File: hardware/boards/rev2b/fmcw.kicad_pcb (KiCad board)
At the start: 4 copper layers, 118.6 x 62 mm, 445 parts, among them CON1 BARREL_JACK, J1 SD_Card, J2 USB_B_Micro, J3 SMA, J4 SMA, J5 SMA, J6 Conn_02x08_Odd_Even, Q1 DNP(RE1C002UN), Q2 RE1C002UN, SW1 SW_PUSH, T1 uwave, T10 uwave, T11 uwave, T12 uwave, T13 uwave, T14 uwave, T15 uwave, T16 uwave, T2 uwave, T3 uwave, T4 uwave, T5 uwave, T6 uwave, T7 uwave, T8 uwave, T9 uwave, U1 LP5907MFX-3.3, U10 LP5907MFX-3.0, U11 LTC2292, U12 ADF4158, U13 TLV172DCK, U14 PS2012GT2-R50, U15 HMC431, U17 PAT1220-C-2DB, U18 SE5004L, U2 LP5907MFX-1.8, U20 PAT1220-C-6DB, U21 LMV321, U22 TRF37A73, U23 SKY65404, U24 TRF37A73, U25 SKY65404, U26 L7980, U27 L7980, U28 L7980, U29 LP2985A-10DBVR, U3 KT2520K-T, U30 TPS7A91, U31 TPS7A91, U32 TPS7A91, U33 LP5907MFX-3.0, U34 TPS7A91, U35 5400BL15B050E, U36 5400BL15B050E, U37 5400BL15B050E, U38 ADL5802, U39 ADA4940-2, U4 NC7SVU04P5X, U40 TPS7A91, U5 NB3N551, U6 XC7A15T-FTG256, U7 MX25L3233F, U8 93LCxxBxxOT, U9 FT2232H, Y1 12MHz

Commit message: rev2b: place silkscreen
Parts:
- moved R21 0.40 mm to (87.5, 105.1)
- moved R20 0.40 mm to (87.5, 104.1)
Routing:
- net /3V3D: track 279.4 -> 280.8 mm
- net GND: vias 901 -> 907

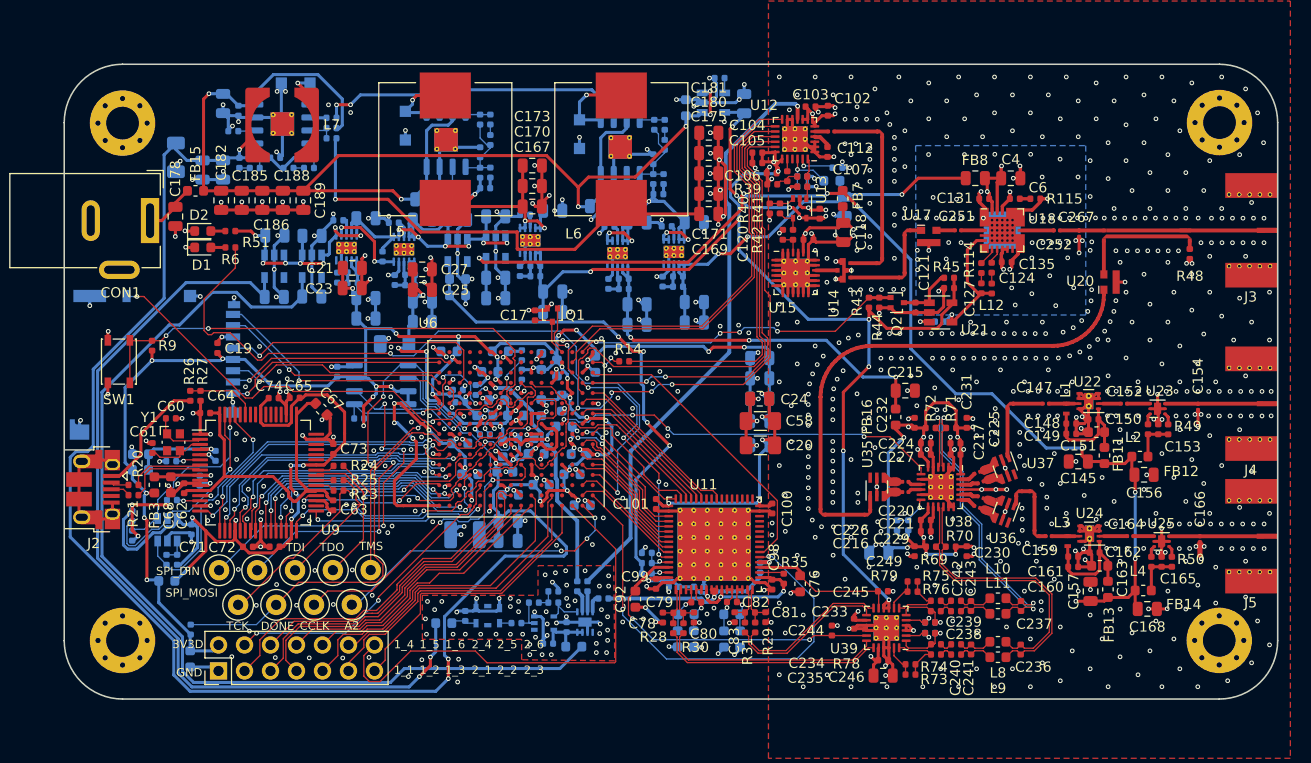
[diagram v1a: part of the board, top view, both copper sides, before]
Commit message: rev2b: add via perimeter
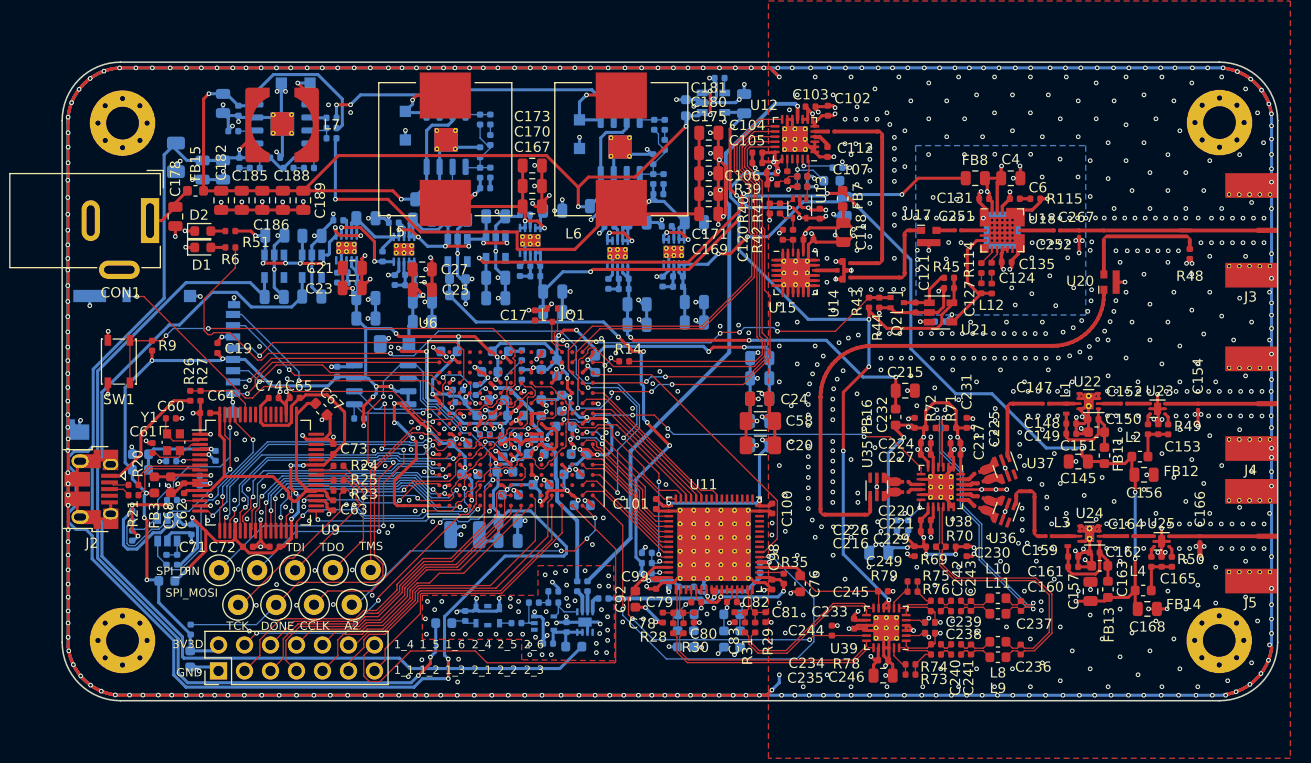
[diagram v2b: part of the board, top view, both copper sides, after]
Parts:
- moved J2 0.17 mm to (83.4, 104.5)
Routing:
- net GND: track 628.9 -> 1189.1 mm, vias 907 -> 1126
- net Net-(C5-Pad1): track 97.9 -> 96.3 mm
- net /1V0: track 165.8 -> 167.0 mm
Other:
- board size 118.6 x 62 mm -> 118.8 x 62.4 mm

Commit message: rev2b: update pcb cost dwg
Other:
- board text added: "PCB cost (OshPark 4-layer): $10/sq.in. x 2.46in. x 4.68in. = $115"
- board text removed: "PCB cost (OshPark 4-layer): $10/sq.in. x 3.28in. x 4.67in. = $153"
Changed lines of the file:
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@@
   (general
     (thickness 1.6002)
-    (drawings 88)
+    (drawings 86)
     (tracks 6130)
     (zones 0)
@@
     (38 B.Mask user hide)
     (39 F.Mask user hide)
-    (40 Dwgs.User user hide)
+    (40 Dwgs.User user)
     (41 Cmts.User user hide)
     (42 Eco1.User user hide)
@@
   (gr_arc (start 193.63 119.45) (end 193.63 125.15) (angle -90) (layer Edge.Cuts) (width 0.15))
   (gr_arc (start 193.63 68.45) (end 199.33 68.45) (angle -90) (layer Edge.Cuts) (width 0.15))
-  (dimension 118.604099 (width 0.127) (layer Dwgs.User)
-    (gr_text "4.6695 in" (at 131.652049 287.8422) (layer Dwgs.User)
-      (effects (font (size 0.8382 0.8382) (thickness 0.127)))
-    )
-    (feature1 (pts (xy 190.954099 265.057269) (xy 190.954099 287.336421)))
-    (feature2 (pts (xy 72.35 265.057269) (xy 72.35 287.336421)))
-    (crossbar (pts (xy 72.35 286.75) (xy 190.954099 286.75)))
-    (arrow1a (pts (xy 190.954099 286.75) (xy 189.827595 287.336421)))
-    (arrow1b (pts (xy 190.954099 286.75) (xy 189.827595 286.163579)))
-    (arrow2a (pts (xy 72.35 286.75) (xy 73.476504 287.336421)))
-    (arrow2b (pts (xy 72.35 286.75) (xy 73.476504 286.163579)))
-  )
-  (dimension 62 (width 0.127) (layer Dwgs.User)
-    (gr_text "2.4409 in" (at 211.646154 242.35 270) (layer Dwgs.User)
-      (effects (font (size 0.8382 0.8382) (thickness 0.127)))
-    )
-    (feature1 (pts (xy 184.95 273.35) (xy 211.140375 273.35)))
-    (feature2 (pts (xy 184.95 211.35) (xy 211.140375 211.35)))
-    (crossbar (pts (xy 210.553954 211.35) (xy 210.553954 273.35)))
-    (arrow1a (pts (xy 210.553954 273.35) (xy 209.967533 272.223496)))
-    (arrow1b (pts (xy 210.553954 273.35) (xy 211.140375 272.223496)))
-    (arrow2a (pts (xy 210.553954 211.35) (xy 209.967533 212.476504)))
-    (arrow2b (pts (xy 210.553954 211.35) (xy 211.140375 212.476504)))
-  )
   (gr_arc (start 86.25 119.45) (end 80.55 119.45) (angle -90) (layer Edge.Cuts) (width 0.15))
   (gr_arc (start 86.25 68.45) (end 86.25 62.75) (angle -90) (layer Edge.Cuts) (width 0.15))
@@
   (gr_line (start 159.654099 90.475262) (end 177.449099 90.475262) (layer F.Mask) (width 0.78))
   (gr_line (start 160.679099 69.985262) (end 160.679099 81.865) (layer F.Mask) (width 0.78))
-  (dimension 118.604099 (width 0.127) (layer Dwgs.User)
-    (gr_text "4.6695 in" (at 137.552049 142.470193) (layer Dwgs.User)
+  (dimension 118.8 (width 0.127) (layer Dwgs.User)
+    (gr_text "4.6772 in" (at 139.95 142.470193) (layer Dwgs.User)
       (effects (font (size 0.8382 0.8382) (thickness 0.127)))
     )
-    (feature1 (pts (xy 196.854099 119.685262) (xy 196.854099 141.964414)))
-    (feature2 (pts (xy 78.25 119.685262) (xy 78.25 141.964414)))
-    (crossbar (pts (xy 78.25 141.377993) (xy 196.854099 141.377993)))
-    (arrow1a (pts (xy 196.854099 141.377993) (xy 195.727595 141.964414)))
-    (arrow1b (pts (xy 196.854099 141.377993) (xy 195.727595 140.791572)))
-    (arrow2a (pts (xy 78.25 141.377993) (xy 79.376504 141.964414)))
-    (arrow2b (pts (xy 78.25 141.377993) (xy 79.376504 140.791572)))
+    (feature1 (pts (xy 199.35 119.685262) (xy 199.35 141.964414)))
+    (feature2 (pts (xy 80.55 119.685262) (xy 80.55 141.964414)))
+    (crossbar (pts (xy 80.55 141.377993) (xy 199.35 141.377993)))
+    (arrow1a (pts (xy 199.35 141.377993) (xy 198.223496 141.964414)))
+    (arrow1b (pts (xy 199.35 141.377993) (xy 198.223496 140.791572)))
+    (arrow2a (pts (xy 80.55 141.377993) (xy 81.676504 141.964414)))
+    (arrow2b (pts (xy 80.55 141.377993) (xy 81.676504 140.791572)))
   )
-  (gr_text "PCB cost (OshPark 4-layer):\n$10/sq.in. x 3.28in. x 4.67in. = $153" (at 78.72 31.17) (layer Dwgs.User)
+  (gr_text "PCB cost (OshPark 4-layer):\n$10/sq.in. x 2.46in. x 4.68in. = $115" (at 101.15 52.65) (layer Dwgs.User)
     (effects (font (size 0.8382 0.8382) (thickness 0.127)))
   )
-  (dimension 83.295 (width 0.127) (layer Dwgs.User)
-    (gr_text "3.279330709 in" (at 231.741264 85.237762 270) (layer Dwgs.User)
+  (dimension 62.4 (width 0.127) (layer Dwgs.User)
+    (gr_text "2.4567 in" (at 231.741264 93.95 270) (layer Dwgs.User)
       (effects (font (size 0.8382 0.8382) (thickness 0.127)))
     )
-    (feature1 (pts (xy 183.549099 126.885262) (xy 231.235485 126.885262)))
-    (feature2 (pts (xy 183.549099 43.590262) (xy 231.235485 43.590262)))
-    (crossbar (pts (xy 230.649064 43.590262) (xy 230.649064 126.885262)))
-    (arrow1a (pts (xy 230.649064 126.885262) (xy 230.062643 125.758758)))
-    (arrow1b (pts (xy 230.649064 126.885262) (xy 231.235485 125.758758)))
-    (arrow2a (pts (xy 230.649064 43.590262) (xy 230.062643 44.716766)))
-    (arrow2b (pts (xy 230.649064 43.590262) (xy 231.235485 44.716766)))
+    (feature1 (pts (xy 183.549099 125.15) (xy 231.235485 125.15)))
+    (feature2 (pts (xy 183.549099 62.75) (xy 231.235485 62.75)))
+    (crossbar (pts (xy 230.649064 62.75) (xy 230.649064 125.15)))
+    (arrow1a (pts (xy 230.649064 125.15) (xy 230.062643 124.023496)))
+    (arrow1b (pts (xy 230.649064 125.15) (xy 231.235485 124.023496)))
+    (arrow2a (pts (xy 230.649064 62.75) (xy 230.062643 63.876504)))
+    (arrow2b (pts (xy 230.649064 62.75) (xy 231.235485 63.876504)))
   )
   (gr_poly (pts (xy 182.89 82.195262) (xy 181.795 82.195262) (xy 181.795 80.295262) (xy 182.89 80.295262)) (layer F.Mask) (width 0))

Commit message: rev2b: add board title silkscreen
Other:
- board text added: "FMCW (rev2b) @matthuszagh"
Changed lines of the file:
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@@
   (general
     (thickness 1.6002)
-    (drawings 86)
+    (drawings 87)
     (tracks 6130)
     (zones 0)
@@
     (35 F.Paste user hide)
     (36 B.SilkS user hide)
-    (37 F.SilkS user hide)
+    (37 F.SilkS user)
     (38 B.Mask user hide)
     (39 F.Mask user hide)
@@
     )
   )
+  (gr_text "FMCW (rev2b)\n@matthuszagh" (at 179.35 67.55) (layer F.SilkS)
+    (effects (font (size 1 1) (thickness 0.15)))
+  )
   (gr_line (start 180.965 79.195262) (end 182.38552 79.195262) (layer F.Mask) (width 0.78))

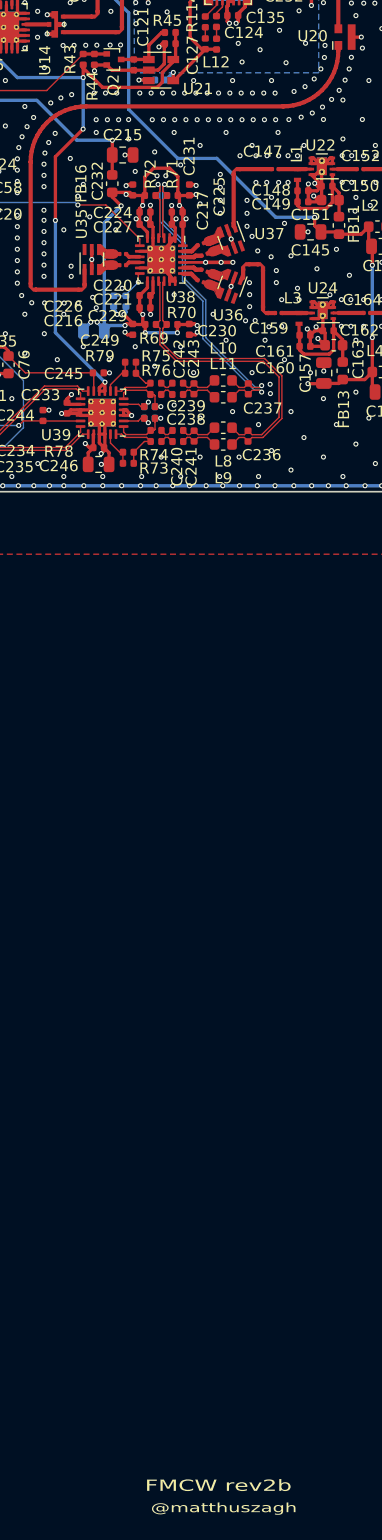
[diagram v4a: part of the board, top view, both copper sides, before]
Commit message: rev2b: add soldermask back to transmission lines
This is a tough choice. ENIG isn't much better than soldermask
apparently and at least we get extra protection with soldermask.
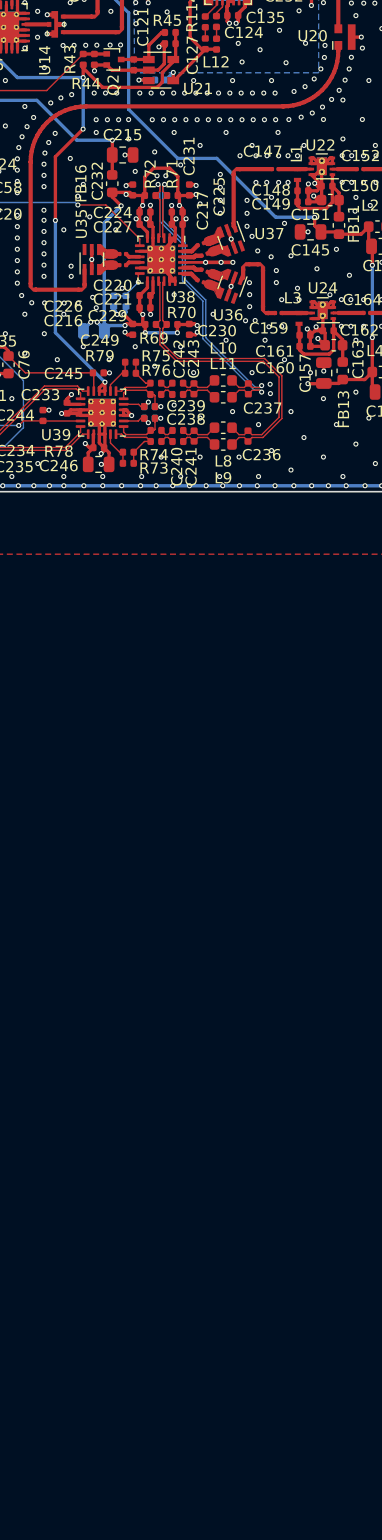
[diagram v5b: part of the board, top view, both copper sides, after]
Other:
- board text removed: "@matthuszagh"
- board text removed: "FMCW rev2b"
